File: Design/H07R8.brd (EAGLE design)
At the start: 34.6 x 90 mm, 80 parts, among them J1 1751248PHOENIX_CONTACT_175124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, J2 1751248PHOENIX_CONTACT_175124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, J3 1751248PHOENIX_CONTACT_175124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, J4 SJ-3524-SMT-TR, P1 HEXABIT_X3_ROW_NO_P4_P6_P7_P8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, Q2 AO3400AALPHA_&_OMEGA_SEMICOND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, U1 STM32G0B1CEU6N, U2 MAX9867ETJ+T, U3 TS3A44159RGTRTEXAS_INSTRUMENT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, U5 MAX9704ETJ+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

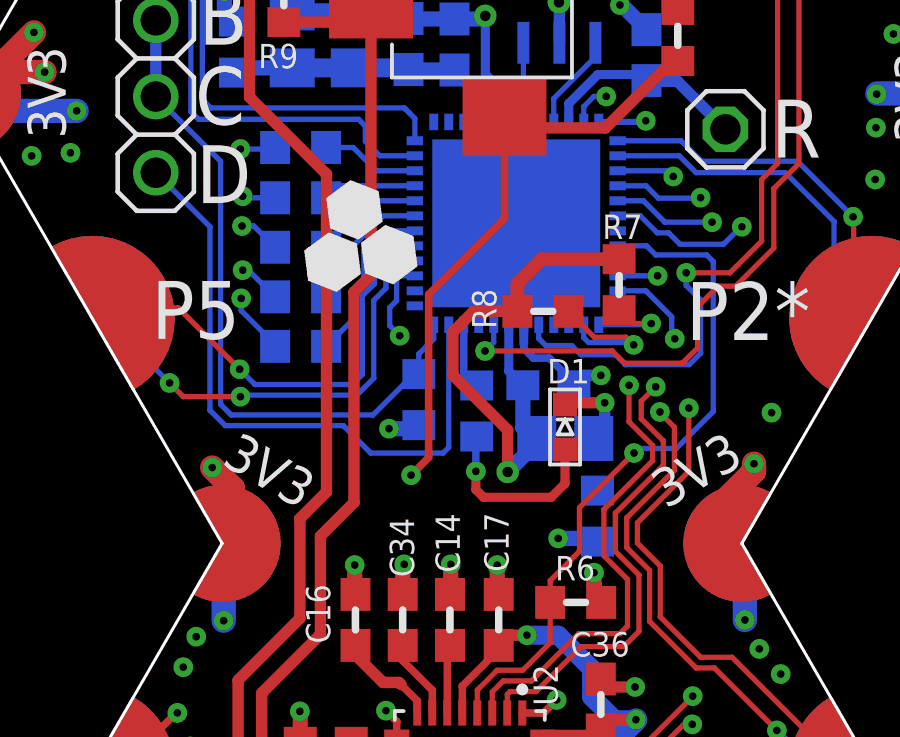
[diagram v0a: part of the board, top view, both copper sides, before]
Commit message: Add TVS diode Edit the logo
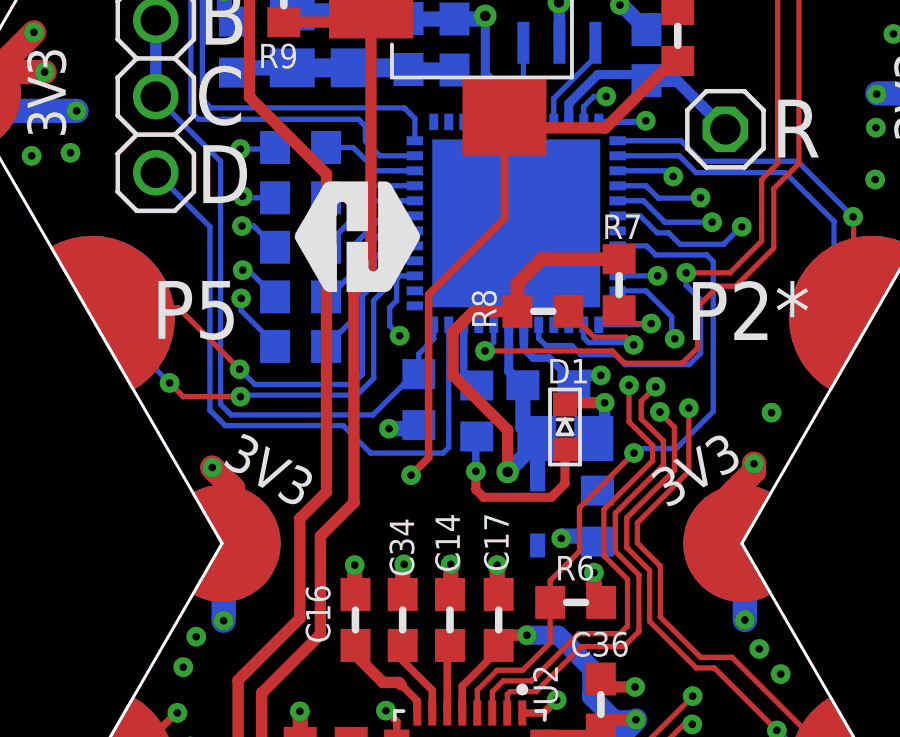
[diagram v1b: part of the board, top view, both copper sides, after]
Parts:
- added D2: BOURNS_CDSOD323-T03SCBOURNS_CDSOD323-T03SC_0_0, HEXABITZ_RCLS:BOURNS_CDSOD323-T03SC_0
- added TRIMBLE-LOGO3: HEXA-LOGO, HEXABITZ_USER_INTERFACE_PARTS:HEXA-LOGO
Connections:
- net GND: now also D2.1
- net VDD: now also D2.2
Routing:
- net VDD: track 71.7 -> 73.1 mm
